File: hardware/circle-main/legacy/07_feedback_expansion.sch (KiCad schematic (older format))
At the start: 5 parts, among them J40 HAPTIC_ACTUATOR, J41 INTERNAL_EXPANSION, J42 EXTERNAL_EXPANSION, U40 DRV2605L, U41 HAPTIC_CURRENT_COMPARATOR

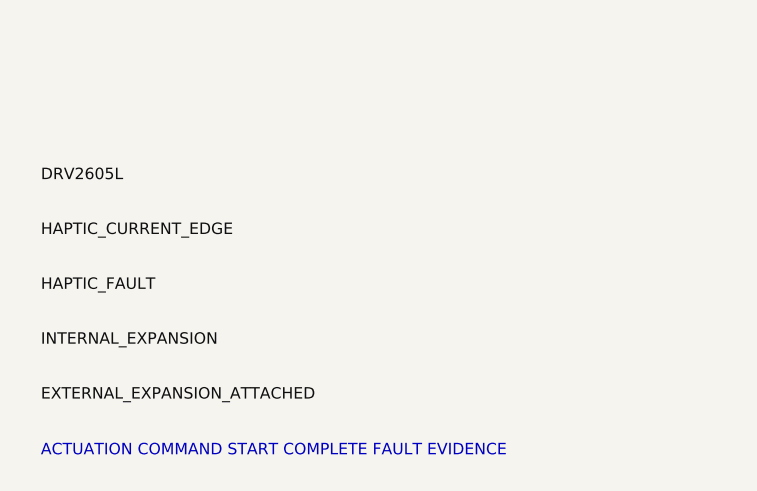
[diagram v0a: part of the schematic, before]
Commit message: Make every CIRCLE review claim reproducible
Validate and export the architecture-level schematics with KiCad 10.0.5, add zero-violation ERC gates, engineering documentation, and one-command evidence hashing.

Constraint: KiCad CLI does not import legacy .sch into native .kicad_sch

Rejected: Hand-written native S-expressions | would create unvalidated CAD

Confidence: medium

Scope-risk: broad

Reversibility: clean

Directive: Treat NET annotations as architecture interfaces, not fabrication-ready connectivity

Tested: py -3.11 tools/verify_release.py; 30 tests; KiCad 10.0.5 ERC/BOM/PDF/SVG/netlist exports

Not-tested: Native conversion, PCB layout, footprints, powered electrodes, human connection, EMC, or regulatory compliance
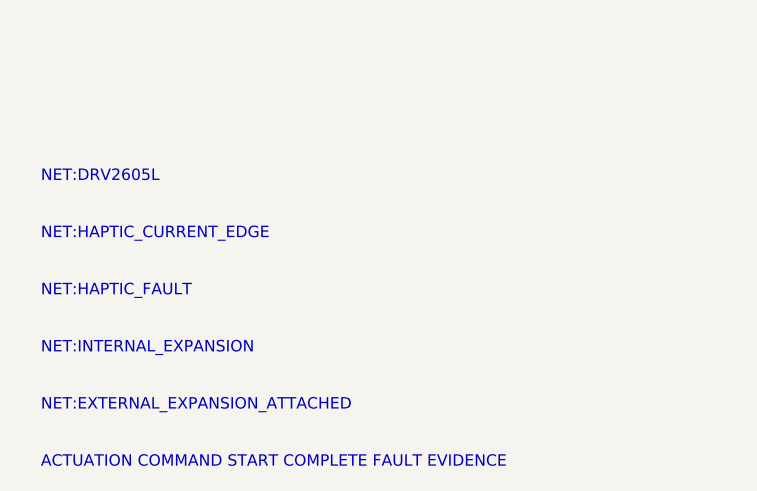
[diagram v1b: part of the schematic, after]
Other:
- note added: "NET:DRV2605L"
- note added: "NET:EXTERNAL_EXPANSION_ATTACHED"
- note added: "NET:HAPTIC_CURRENT_EDGE"
- note added: "NET:HAPTIC_FAULT"
- note added: "NET:INTERNAL_EXPANSION"
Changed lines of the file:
@@
 Sheet 1 1
 Title "Haptic and expansion"
+Date "2026-08-14"
+Rev "A"
+Comp "Vers3Dynamics"
 Comment1 "ENGINEERING REVIEW ONLY - NOT FOR HUMAN CONNECTION"
+Comment2 "Generated artifact - edit manifest/generator"
+Comment3 ""
+Comment4 ""
 $EndDescr
 $Comp
@@
 F 0 "U40" H 1400 1300 50  0000 C CNN
 F 1 "DRV2605L" H 1400 1100 50  0000 C CNN
+F 2 "" H 1300 1200 50  0001 C CNN
+F 3 "" H 1300 1200 50  0001 C CNN
+	1    1300 1200
 	1    0    0    -1
 $EndComp
@@
 F 0 "U41" H 3500 1300 50  0000 C CNN
 F 1 "HAPTIC_CURRENT_COMPARATOR" H 3500 1100 50  0000 C CNN
+F 2 "" H 3400 1200 50  0001 C CNN
+F 3 "" H 3400 1200 50  0001 C CNN
+	1    3400 1200
 	1    0    0    -1
 $EndComp
@@
 F 0 "J40" H 5600 1300 50  0000 C CNN
 F 1 "HAPTIC_ACTUATOR" H 5600 1100 50  0000 C CNN
+F 2 "" H 5500 1200 50  0001 C CNN
+F 3 "" H 5500 1200 50  0001 C CNN
+	1    5500 1200
 	1    0    0    -1
 $EndComp
@@
 F 0 "J41" H 7700 1300 50  0000 C CNN
 F 1 "INTERNAL_EXPANSION" H 7700 1100 50  0000 C CNN
+F 2 "" H 7600 1200 50  0001 C CNN
+F 3 "" H 7600 1200 50  0001 C CNN
+	1    7600 1200
 	1    0    0    -1
 $EndComp
@@
 F 0 "J42" H 1400 2100 50  0000 C CNN
 F 1 "EXTERNAL_EXPANSION" H 1400 1900 50  0000 C CNN
+F 2 "" H 1300 2000 50  0001 C CNN
+F 3 "" H 1300 2000 50  0001 C CNN
+	1    1300 2000
 	1    0    0    -1
 $EndComp
-Text Label 700 5600 0    50   ~ 0
-DRV2605L
-Text Label 700 5840 0    50   ~ 0
-HAPTIC_CURRENT_EDGE
-Text Label 700 6080 0    50   ~ 0
-HAPTIC_FAULT
-Text Label 700 6320 0    50   ~ 0
-INTERNAL_EXPANSION
-Text Label 700 6560 0    50   ~ 0
-EXTERNAL_EXPANSION_ATTACHED
 Text Notes 600 400 0    50   ~ 0
 ENGINEERING REVIEW ONLY - NOT FOR HUMAN CONNECTION
-Text Notes 700 6800 0    50   ~ 0
+Text Notes 700 5600 0    50   ~ 0
+NET:DRV2605L
+Text Notes 700 5850 0    50   ~ 0
+NET:HAPTIC_CURRENT_EDGE
+Text Notes 700 6100 0    50   ~ 0
+NET:HAPTIC_FAULT
+Text Notes 700 6350 0    50   ~ 0
+NET:INTERNAL_EXPANSION
+Text Notes 700 6600 0    50   ~ 0
+NET:EXTERNAL_EXPANSION_ATTACHED
+Text Notes 700 6850 0    50   ~ 0
 ACTUATION COMMAND START COMPLETE FAULT EVIDENCE
 $EndSCHEMATC
